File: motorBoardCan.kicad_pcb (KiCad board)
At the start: 6 copper layers, 50 x 50 mm, 71 parts, among them J1 Conn_01x04_Pin, J10 Conn_01x02_Pin, J11 Conn_01x02_Pin, J12 Conn_01x02_Pin, J2 Conn_01x04_Pin, J3 Conn_02x04_Top_Bottom, J4 Conn_01x02_Pin, J5 Conn_01x02_Pin, J6 Conn_02x04_Top_Bottom, J7 Conn_01x02_Pin, J8 Conn_01x02_Pin, J9 Conn_01x02_Pin, Q1 AO3400A, Q2 AO3400A, Q3 AO3400A, Q4 AO3400A, U1 NUCLEO-G431KB, U10 TPS563200, U4 SN65HVD230, U5 LD1117S33TR_SOT223

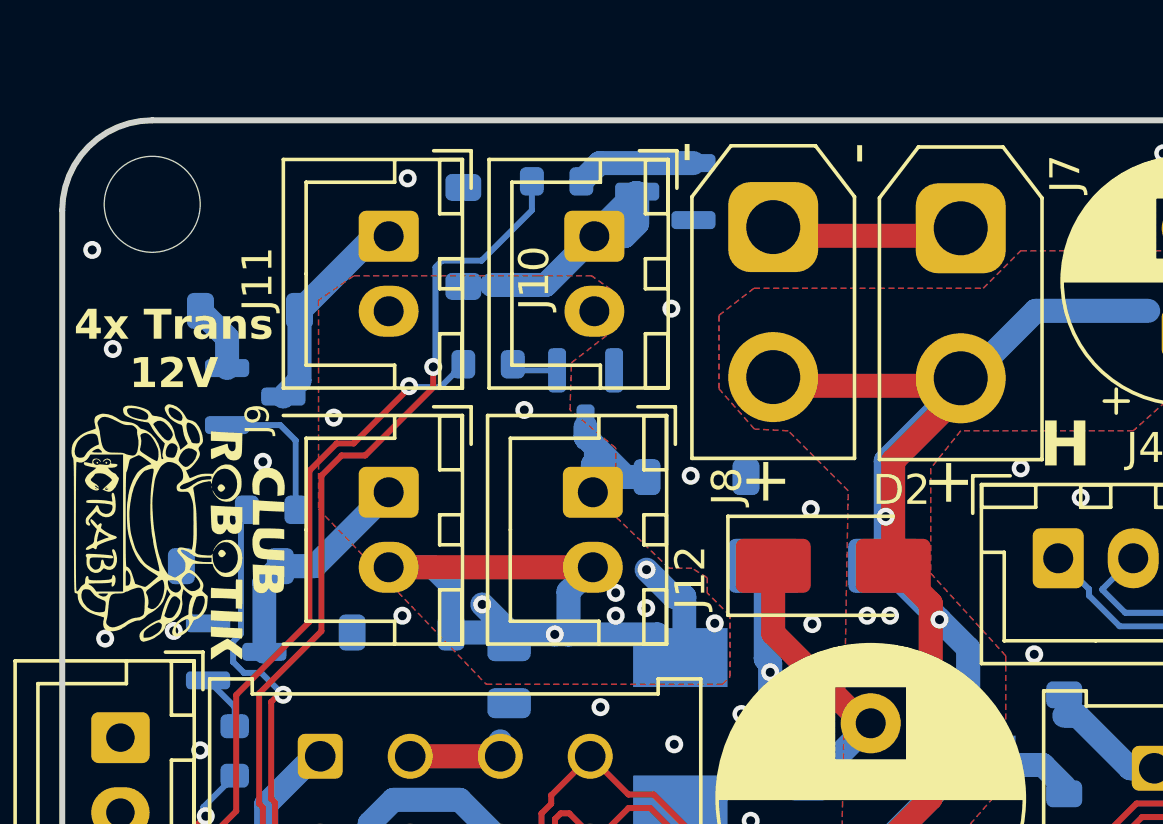
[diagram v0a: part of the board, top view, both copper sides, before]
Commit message: fix transistor by adding a correct free-wheeling diode
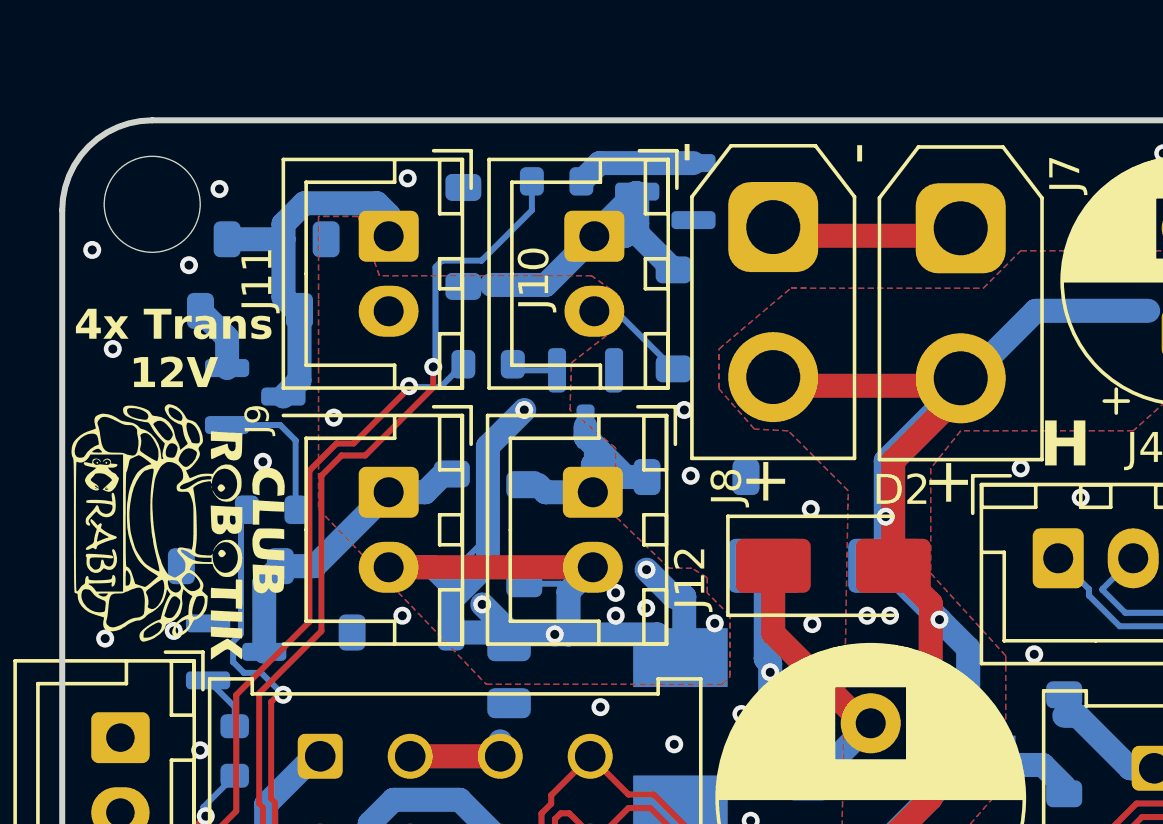
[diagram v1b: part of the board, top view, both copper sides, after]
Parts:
- added D10: D_transistor, Diode_SMD:D_SOD-123, B.Cu at (89.8, 70.8)
- added D11: D_transistor, Diode_SMD:D_SOD-123, B.Cu at (97.2, 64.0)
- added D12: D_transistor, Diode_SMD:D_SOD-123, B.Cu at (83.9, 61.4)
- added D13: D_transistor, Diode_SMD:D_SOD-123, B.Cu at (92.2, 71.2)
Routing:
- net 12V: track 27.2 -> 40.4 mm
- net Net-(D12-A): track 7.08 -> 12.3 mm
- net Net-(D10-A): track 7.76 -> 9.84 mm
- net Net-(D11-A): track 8.77 -> 10.8 mm
- net Net-(D13-A): track 5.68 -> 7.62 mm
- net GND: vias 75 -> 77
